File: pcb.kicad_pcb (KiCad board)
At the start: 2 copper layers, 120.7 x 70.6 mm, 50 parts, among them SW1 SW_Push, SW2 SW_Push, U1 Pico

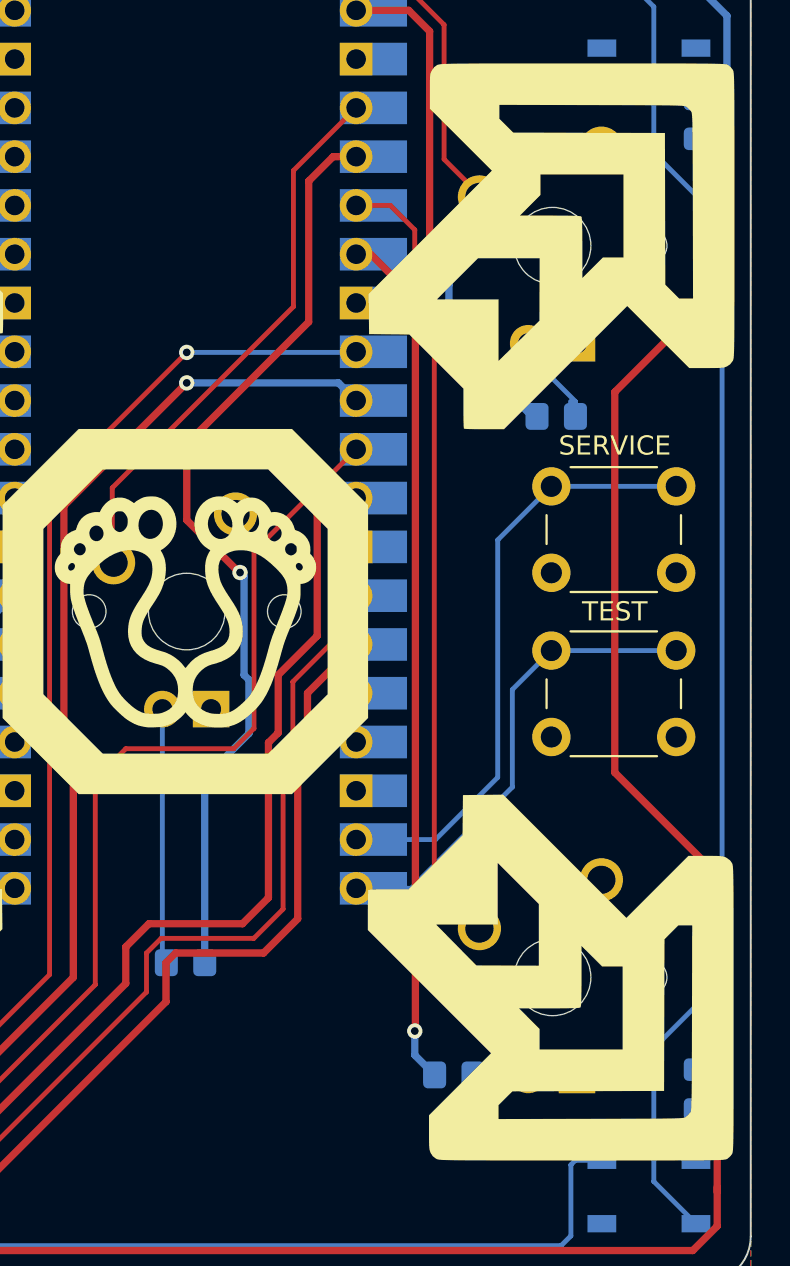
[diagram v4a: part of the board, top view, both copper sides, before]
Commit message: Add test/service buttons to plate, begin renaming
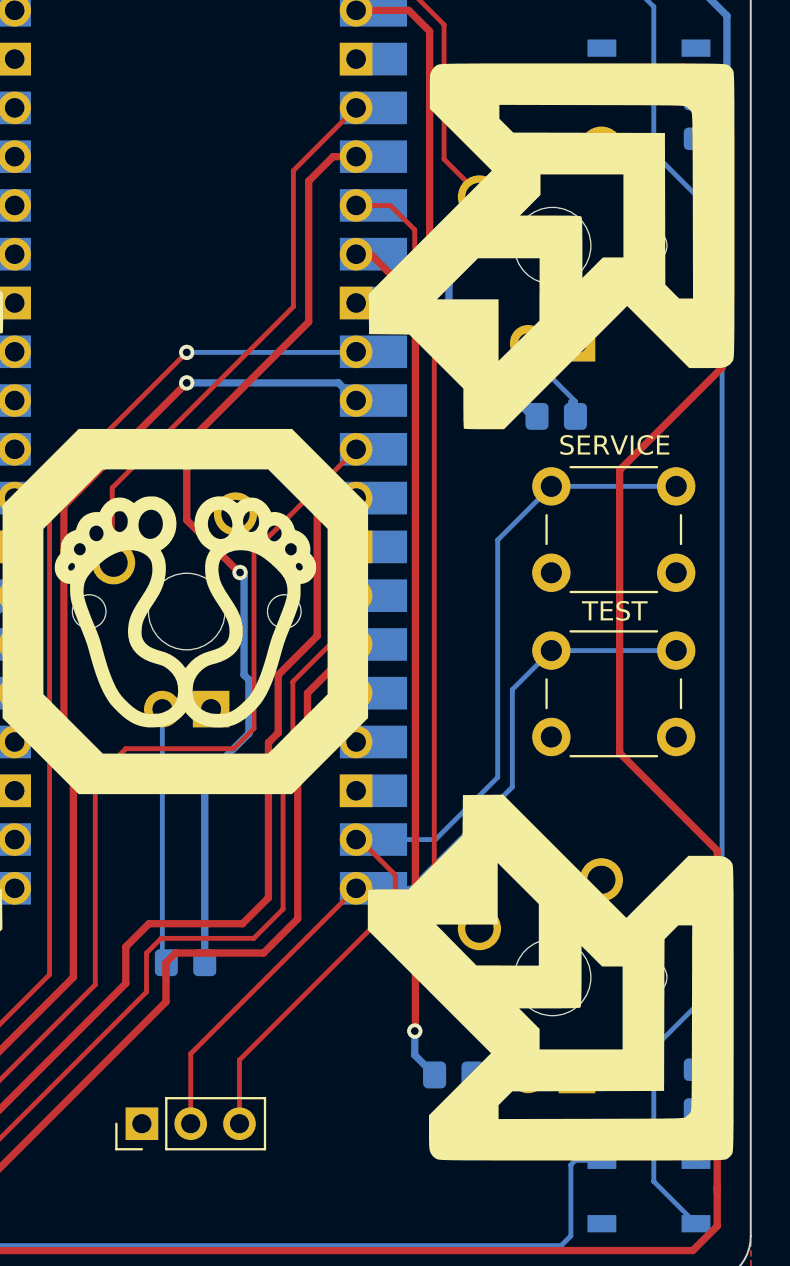
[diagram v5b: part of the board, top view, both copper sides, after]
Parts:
- added REF**: PinHeader_1x03_P2.54mm_Vertical, Connector_PinHeader_2.54mm:PinHeader_1x03_P2.54mm_Vertical, F.Cu at (170.7, 121.9)
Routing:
- net SERVICE: track 31.5 -> 50.6 mm
- net TEST: track 24.8 -> 40.6 mm
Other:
- board text added: "PicoFX PCB Rev. 2 https://github.com/dj505/PicoFX"
- board text removed: "HandPump PCB Rev. 2 https://github.com/dj505/handpump"
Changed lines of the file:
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@@
       ) (layer "F.SilkS") (width 0) (fill solid))
   )
+  (footprint "Connector_PinHeader_2.54mm:PinHeader_1x03_P2.54mm_Vertical" (layer "F.Cu")
+    (at 170.703 121.92 90)
+    (descr "Through hole straight pin header, 1x03, 2.54mm pitch, single row")
+    (tags "Through hole pin header THT 1x03 2.54mm single row")
+    (attr through_hole)
+    (fp_text reference "REF**" (at 0 -2.33 90) (layer "F.SilkS") hide
+      (effects (font (size 1 1) (thickness 0.15)))
+    )
+    (fp_text value "PinHeader_1x03_P2.54mm_Vertical" (at 0 7.41 90) (layer "F.Fab") hide
+      (effects (font (size 1 1) (thickness 0.15)))
+    )
+    (fp_text user "${REFERENCE}" (at 0 2.54) (layer "F.Fab") hide
+      (effects (font (size 1 1) (thickness 0.15)))
+    )
+    (fp_line (start 1.33 1.27) (end 1.33 6.41) (layer "F.SilkS") (width 0.12))
+    (fp_line (start -1.33 1.27) (end -1.33 6.41) (layer "F.SilkS") (width 0.12))
+    (fp_line (start -1.33 1.27) (end 1.33 1.27) (layer "F.SilkS") (width 0.12))
+    (fp_line (start -1.33 -1.33) (end 0 -1.33) (layer "F.SilkS") (width 0.12))
+    (fp_line (start -1.33 6.41) (end 1.33 6.41) (layer "F.SilkS") (width 0.12))
+    (fp_line (start -1.33 0) (end -1.33 -1.33) (layer "F.SilkS") (width 0.12))
+    (fp_line (start -1.8 6.85) (end 1.8 6.85) (layer "F.CrtYd") (width 0.05))
+    (fp_line (start 1.8 6.85) (end 1.8 -1.8) (layer "F.CrtYd") (width 0.05))
+    (fp_line (start -1.8 -1.8) (end -1.8 6.85) (layer "F.CrtYd") (width 0.05))
+    (fp_line (start 1.8 -1.8) (end -1.8 -1.8) (layer "F.CrtYd") (width 0.05))
+    (fp_line (start 1.27 6.35) (end -1.27 6.35) (layer "F.Fab") (width 0.1))
+    (fp_line (start -1.27 -0.635) (end -0.635 -1.27) (layer "F.Fab") (width 0.1))
+    (fp_line (start -0.635 -1.27) (end 1.27 -1.27) (layer "F.Fab") (width 0.1))
+    (fp_line (start -1.27 6.35) (end -1.27 -0.635) (layer "F.Fab") (width 0.1))
+    (fp_line (start 1.27 -1.27) (end 1.27 6.35) (layer "F.Fab") (width 0.1))
+    (pad "1" thru_hole rect (at 0 0 90) (size 1.7 1.7) (drill 1) (layers *.Cu *.Mask)
+      (net 2 "GND"))
+    (pad "2" thru_hole oval (at 0 2.54 90) (size 1.7 1.7) (drill 1) (layers *.Cu *.Mask)
+      (net 33 "TEST"))
+    (pad "3" thru_hole oval (at 0 5.08 90) (size 1.7 1.7) (drill 1) (layers *.Cu *.Mask)
+      (net 32 "SERVICE"))
+    (model "${KICAD6_3DMODEL_DIR}/Connector_PinHeader_2.54mm.3dshapes/PinHeader_1x03_P2.54mm_Vertical.wrl"
+      (offset (xyz 0 0 0))
+      (scale (xyz 1 1 1))
+      (rotate (xyz 0 0 0))
+    )
+  )
   (footprint "Button_Switch_THT:SW_PUSH_6mm" (layer "F.Cu")
     (at 192.024 88.732)
@@
     (effects (font (size 1 1) (thickness 0.15)))
   )
-  (gr_text "HandPump PCB Rev. 2\nhttps://github.com/dj505/handpump" (at 189.23 125.73) (layer "B.Mask")
+  (gr_text "PicoFX PCB Rev. 2\nhttps://github.com/dj505/PicoFX" (at 189.23 125.73) (layer "B.Mask")
     (effects (font (size 1.016 1.016) (thickness 0.15)) (justify left mirror))
   )
@@
   (segment (start 199.39 128.524) (end 200.66 127.254) (width 0.381) (layer "F.Cu") (net 1))
   (segment (start 93.218 61.214) (end 85.852 61.214) (width 0.381) (layer "F.Cu") (net 1))
-  (segment (start 195.326 83.82) (end 195.326 103.632) (width 0.381) (layer "F.Cu") (net 1))
+  (segment (start 200.914 69.596) (end 200.914 82.55) (width 0.381) (layer "F.Cu") (net 1))
   (segment (start 91.186 125.222) (end 86.106 125.222) (width 0.381) (layer "F.Cu") (net 1))
-  (segment (start 199.644 70.866) (end 199.644 79.502) (width 0.381) (layer "F.Cu") (net 1))
   (segment (start 86.106 125.222) (end 83.566 122.682) (width 0.381) (layer "F.Cu") (net 1))
   (segment (start 141.859 128.524) (end 85.09 128.524) (width 0.381) (layer "F.Cu") (net 1))
-  (segment (start 200.914 69.596) (end 199.644 70.866) (width 0.381) (layer "F.Cu") (net 1))
-  (segment (start 199.644 79.502) (end 195.326 83.82) (width 0.381) (layer "F.Cu") (net 1))
   (segment (start 144.907 125.476) (end 141.859 128.524) (width 0.381) (layer "F.Cu") (net 1))
   (segment (start 146.558 61.468) (end 146.812 61.214) (width 0.381) (layer "F.Cu") (net 1))
@@
   (segment (start 146.558 61.468) (end 146.304 61.214) (width 0.381) (layer "F.Cu") (net 1))
   (segment (start 163.888752 61.214) (end 164.07775 61.402998) (width 0.381) (layer "F.Cu") (net 1))
+  (segment (start 200.66 107.696) (end 200.66 122.682) (width 0.381) (layer "F.Cu") (net 1))
   (segment (start 86.36 94.996) (end 83.566 92.202) (width 0.381) (layer "F.Cu") (net 1))
-  (segment (start 200.66 108.966) (end 200.66 122.682) (width 0.381) (layer "F.Cu") (net 1))
+  (segment (start 200.914 82.55) (end 195.58 87.884) (width 0.381) (layer "F.Cu") (net 1))
   (segment (start 146.812 61.214) (end 163.888752 61.214) (width 0.381) (layer "F.Cu") (net 1))
   (segment (start 83.566 63.5) (end 83.566 92.202) (width 0.381) (layer "F.Cu") (net 1))
@@
   (segment (start 145.034 125.476) (end 144.907 125.476) (width 0.381) (layer "F.Cu") (net 1))
   (segment (start 139.954 128.524) (end 199.39 128.524) (width 0.381) (layer "F.Cu") (net 1))
+  (segment (start 195.58 87.884) (end 195.58 102.616) (width 0.381) (layer "F.Cu") (net 1))
   (segment (start 94.234 61.214) (end 93.218 61.214) (width 0.381) (layer "F.Cu") (net 1))
   (segment (start 200.66 127.254) (end 200.66 125.222) (width 0.381) (layer "F.Cu") (net 1))
-  (segment (start 195.326 103.632) (end 200.66 108.966) (width 0.381) (layer "F.Cu") (net 1))
+  (segment (start 195.58 102.616) (end 200.66 107.696) (width 0.381) (layer "F.Cu") (net 1))
   (via (at 145.034 125.476) (size 0.8) (drill 0.4) (layers "F.Cu" "B.Cu") (net 1))
   (via (at 200.914 69.596) (size 0.8) (drill 0.4) (layers "F.Cu" "B.Cu") (net 1))
@@
   (segment (start 178.054 110.744) (end 176.53 112.268) (width 0.254) (layer "F.Cu") (net 29))
   (segment (start 181.85775 94.422998) (end 180.594 95.686748) (width 0.254) (layer "F.Cu") (net 29))
+  (segment (start 175.783 118.603) (end 183.896 110.49) (width 0.254) (layer "F.Cu") (net 32))
+  (segment (start 182.052998 107.122998) (end 181.85775 107.122998) (width 0.254) (layer "F.Cu") (net 32))
+  (segment (start 175.783 121.92) (end 175.783 118.603) (width 0.254) (layer "F.Cu") (net 32))
+  (segment (start 183.896 108.966) (end 182.052998 107.122998) (width 0.254) (layer "F.Cu") (net 32))
+  (segment (start 183.896 110.49) (end 183.896 108.966) (width 0.254) (layer "F.Cu") (net 32))
   (segment (start 189.23 103.886) (end 185.993002 107.122998) (width 0.254) (layer "B.Cu") (net 32))
   (segment (start 192.024 88.732) (end 189.23 91.526) (width 0.254) (layer "B.Cu") (net 32))
@@
   (segment (start 192.024 88.732) (end 198.524 88.732) (width 0.254) (layer "B.Cu") (net 32))
   (segment (start 185.993002 107.122998) (end 181.85775 107.122998) (width 0.254) (layer "B.Cu") (net 32))
+  (segment (start 173.243 118.277748) (end 181.85775 109.662998) (width 0.254) (layer "F.Cu") (net 33))
+  (segment (start 173.243 121.92) (end 173.243 118.277748) (width 0.254) (layer "F.Cu") (net 33))
   (segment (start 189.992 99.314) (end 189.992 104.394) (width 0.254) (layer "B.Cu") (net 33))
   (segment (start 192.024 97.282) (end 198.524 97.282) (width 0.254) (layer "B.Cu") (net 33))

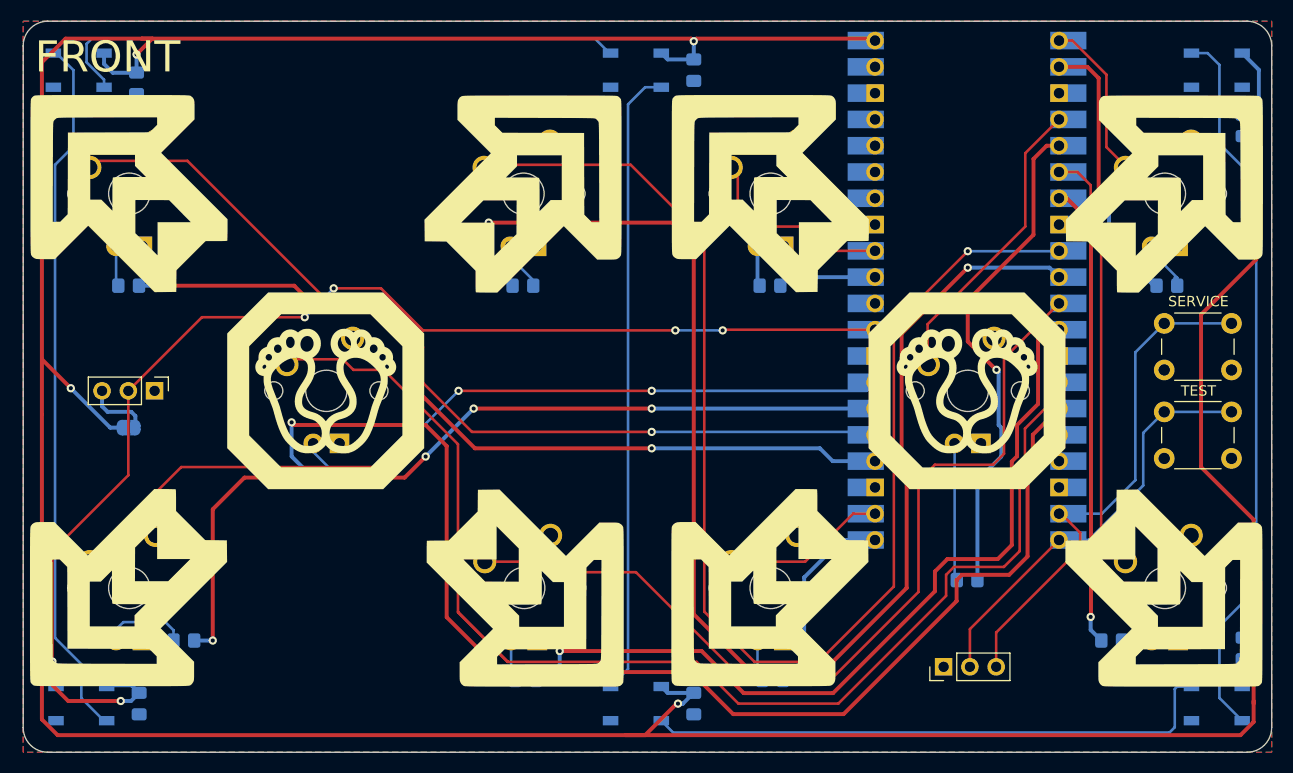
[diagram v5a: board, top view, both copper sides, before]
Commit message: Use 90 degree buttons for test/service, smol fixes
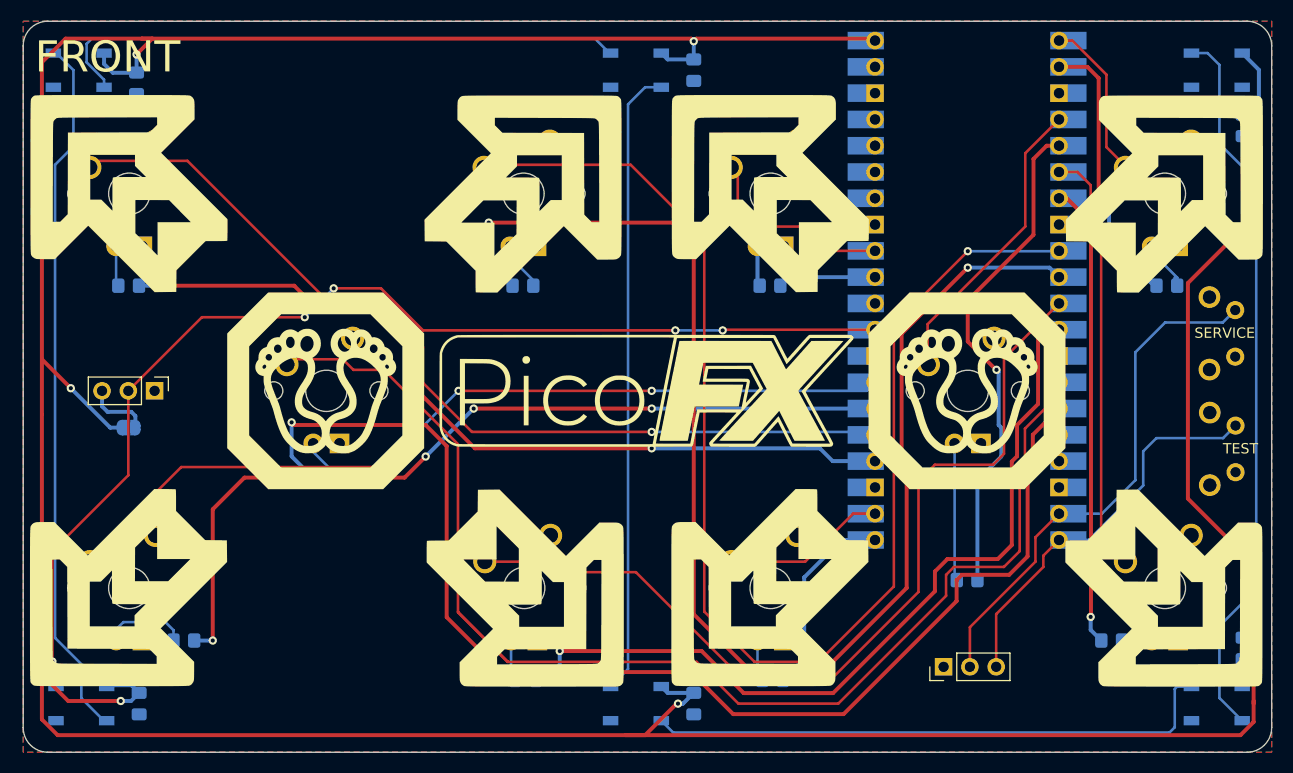
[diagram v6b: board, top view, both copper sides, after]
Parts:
- removed SW1, SW2: SW_Push, Button_Switch_THT:SW_PUSH_6mm
- added G***: LOGO, LogoFootprints:PicoFX, F.Cu at (142.0, 95.2)
- added REF**: SW_Tactile_SPST_Angled_PTS645Vx39-2LFS, Button_Switch_THT:SW_Tactile_SPST_Angled_PTS645Vx39-2LFS, B.Cu at (198.9, 91.9)
- added REF**: SW_Tactile_SPST_Angled_PTS645Vx39-2LFS, Button_Switch_THT:SW_Tactile_SPST_Angled_PTS645Vx39-2LFS, B.Cu at (198.9, 103.1)
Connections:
- REF** pad 2: TEST -> SERVICE
- REF** pad 3: SERVICE -> TEST
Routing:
- net TEST: track 40.6 -> 38.3 mm
- net +5V: track 396.3 -> 397.4 mm
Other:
- board text added: "PicoFX PCB Rev. 3 https://github.com/dj505/PicoFX"
- board text removed: "PicoFX PCB Rev. 2 https://github.com/dj505/PicoFX"

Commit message: Fix P1 UL/DL being swapped
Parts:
- C1, C2, C3, C4, C5, C6: value 1000uF -> 100uF
- moved MX1 38.1 mm to (92.0, 114.3)
- moved MX2 38.1 mm to (92.0, 76.2)
- moved R1 34.7 mm to (97.3, 119.4)
- moved R2 34.7 mm to (91.9, 85.1)
- renumbered MX2 to MX1, MX1 to MX2
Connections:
- U1 pad 24: P1 DL LED -> P1 UL LED
- U1 pad 25: P1 DL -> P1 UL
- U1 pad 26: P1 UL LED -> P1 DL LED
- U1 pad 27: P1 UL -> P1 DL
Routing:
- net P1 UL: track 83.1 -> 89.1 mm, vias 3 -> 1
- net P1 DL: track 89.1 -> 83.1 mm, vias 1 -> 3
- net Net-(MX2-Pad3): track 8.23 -> 3.90 mm
- net Net-(MX1-Pad3): track 3.90 -> 8.23 mm
- net P1 UL LED: track 82.5 -> 80.1 mm, vias 4 -> 2
- net P1 DL LED: track 80.1 -> 82.5 mm, vias 2 -> 4
